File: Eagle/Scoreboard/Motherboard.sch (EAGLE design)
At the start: 24 parts

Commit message: Changed transistor type for score controller, changed number of terminals to 8. Motherboard still TBD
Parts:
- removed DISP_POWER: (no value), con-wago-500:W237-102
- added 12V, LED: (no value), con-wago-500:W237-102
- added R7: 470, resistor:R-EU_0204/5
- added SG1: EB2505, buzzer:EB2505
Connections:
- new net 12V: 12V-1.KL, 12V-2.KL, C1.+, R7.2, REG.VI, VCC-1.KL
- net GND: now also LED-1.KL; no longer DISP_POWER-1.KL
- net N$7: now also LED-2.KL, R7.1; no longer C1.+, REG.VI, VCC-1.KL
- net VCC: no longer DISP_POWER-2.KL

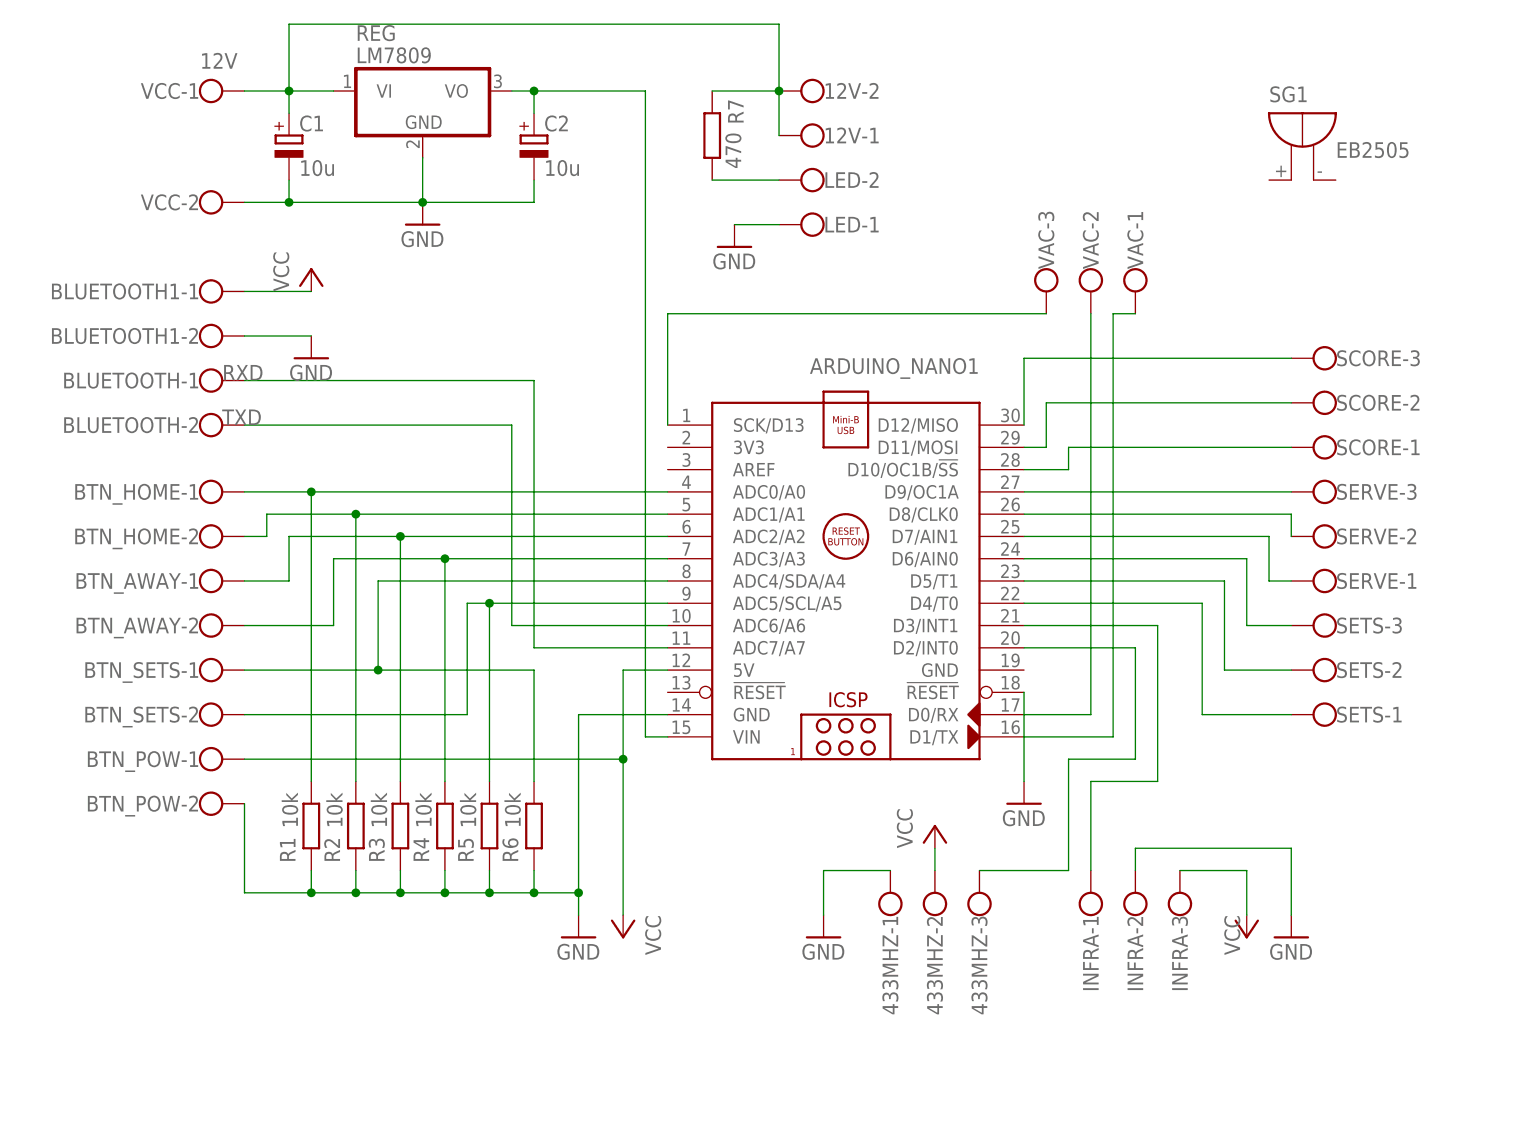
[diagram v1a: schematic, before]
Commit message: Changed matherboard scheme and start designing PCB
Scheme was changed to make easier PCB design. Still need to finish VCC layer on TOP layer
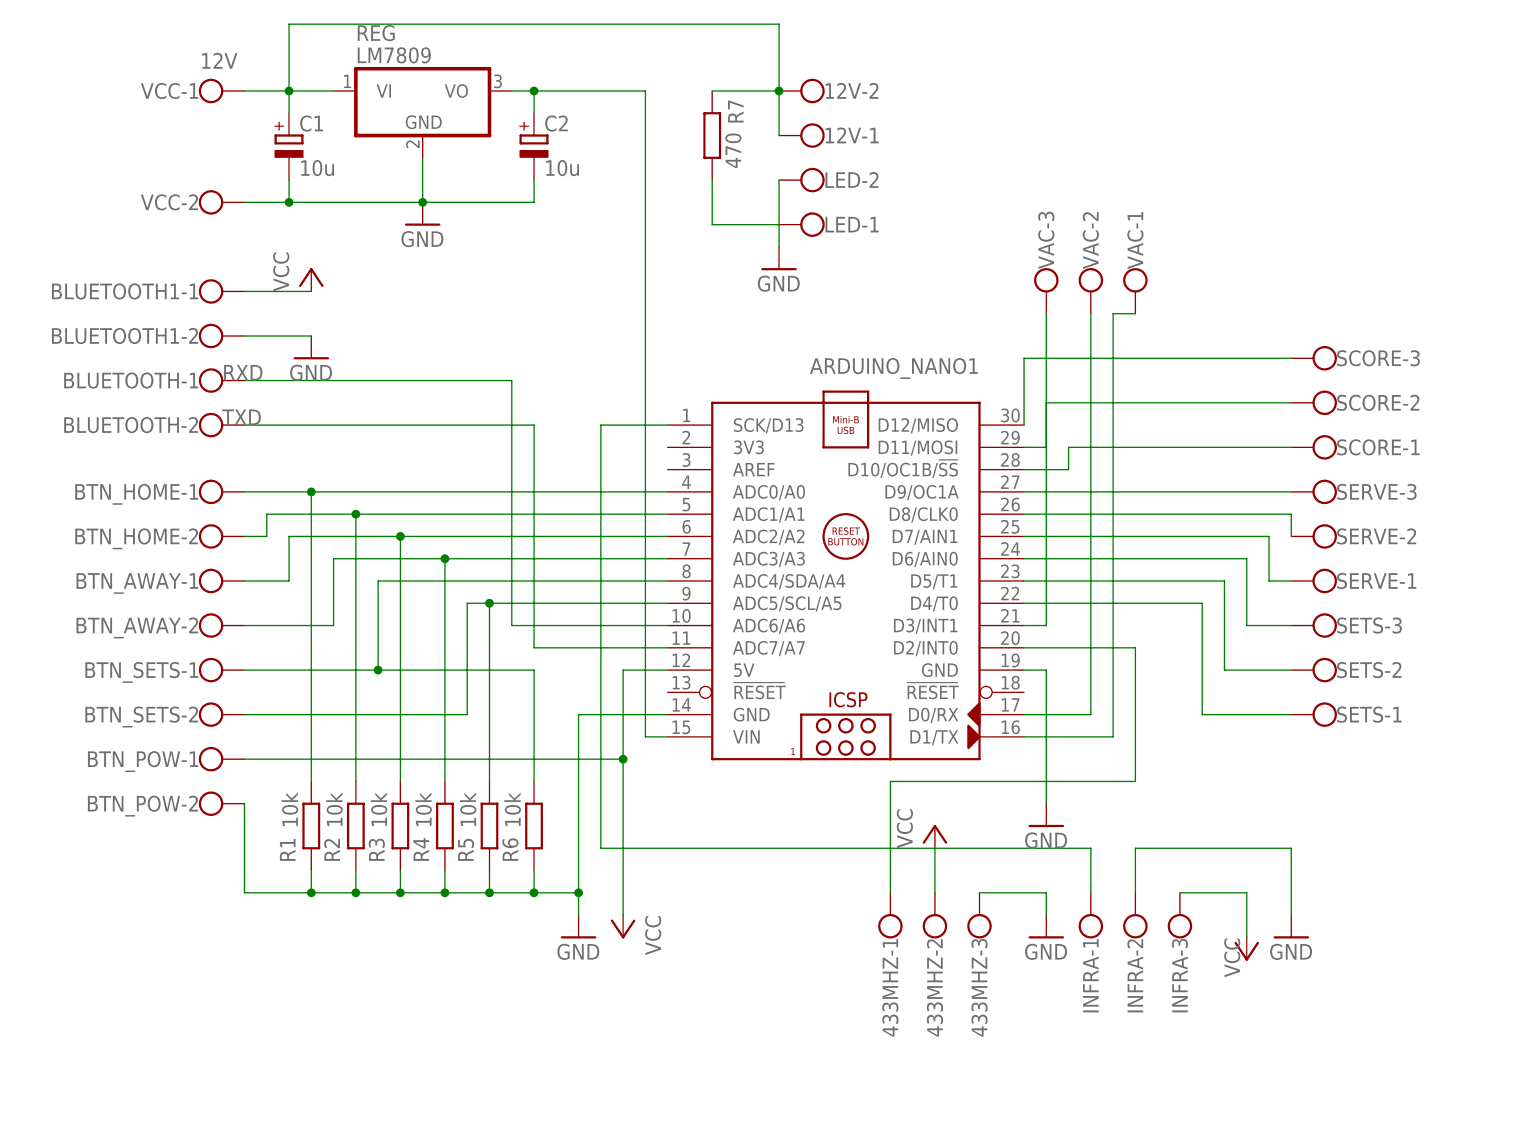
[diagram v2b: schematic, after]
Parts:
- removed SG1: EB2505, buzzer:EB2505
- R1, R2, R3, R4, R5, R6, R7: device resistor:R-EU_0204/5 -> resistor:R-EU_0204/7
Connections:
- net N$22 renamed VAC1
- net N$23 renamed VAC2
- removed net N$19: 433MHZ-3.KL, ARDUINO_NANO1.D2/INT0
- removed net N$20: ARDUINO_NANO1.D3/INT1, INFRA-1.KL
- removed net N$24: ARDUINO_NANO1.SCK/D13, VAC-3.KL
- removed net N$8: ARDUINO_NANO1.ADC6/A6, BLUETOOTH-2.KL
- removed net N$9: ARDUINO_NANO1.ADC7/A7, BLUETOOTH-1.KL
- new net 433MHZ: 433MHZ-1.KL, ARDUINO_NANO1.D2/INT0
- new net INFRA: ARDUINO_NANO1.SCK/D13, INFRA-1.KL
- new net RXD: ARDUINO_NANO1.ADC7/A7, BLUETOOTH-2.KL
- new net TXD: ARDUINO_NANO1.ADC6/A6, BLUETOOTH-1.KL
- new net VAC3: ARDUINO_NANO1.D3/INT1, VAC-3.KL
- net GND: now also 433MHZ-3.KL, ARDUINO_NANO1.GND@1, LED-2.KL; no longer 433MHZ-1.KL, ARDUINO_NANO1.!RESET@1, LED-1.KL
- net N$7: now also LED-1.KL; no longer LED-2.KL
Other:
- moved on the sheet: 433MHZ-1, 433MHZ-2, 433MHZ-3, INFRA-1, INFRA-2, INFRA-3

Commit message: Finalized board for motherboard
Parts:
- removed 433MHZ, INFRA: (no value), con-wago-500:W237-103
- added 433MHZ_VC, INFRA_VC, SIGNAL_IN: (no value), con-wago-500:W237-102
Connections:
- net N$10 renamed SCORE_3
- net N$11 renamed SCORE_2
- net N$12 renamed SCORE_1
- net N$13 renamed SERVE_3
- net N$14 renamed SERVE_2
- net N$15 renamed SERVE_1
- net N$16 renamed SETS_3
- net N$17 renamed SETS_2
- net N$18 renamed SETS_1
- net VIN renamed VIN_9V
- removed net VAC2: ARDUINO_NANO1.D0/RX, VAC-2.KL
- new net RESET: ARDUINO_NANO1.!RESET@1, VAC-2.KL
- net 433MHZ: now also SIGNAL_IN-1.KL; no longer 433MHZ-1.KL
- net GND: now also 433MHZ_VC-1.KL, INFRA_VC-2.KL; no longer 433MHZ-3.KL, INFRA-2.KL
- net INFRA: now also SIGNAL_IN-2.KL; no longer INFRA-1.KL
- net VCC: now also 433MHZ_VC-2.KL, INFRA_VC-1.KL; no longer 433MHZ-2.KL, INFRA-3.KL
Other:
- note added: "433 MHz"
- note added: "Infra"
- moved on the sheet: VAC-1, VAC-2, VAC-3

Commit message: Added capacitors for filtering
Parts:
- added C3, C4: 100n, capacitor-wima:C5/2.5
- C2: value 10u -> 47u
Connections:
- net 12V: now also C3.1
- net GND: now also C3.2, C4.2
- net VIN_9V: now also C4.1
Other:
- moved on the sheet: C1
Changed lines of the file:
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@@
 <part name="GND2" library="supply1" library_urn="urn:adsk.eagle:library:371" deviceset="GND" device=""/>
 <part name="C1" library="rcl" library_urn="urn:adsk.eagle:library:334" deviceset="CPOL-EU" device="E2-4" package3d_urn="urn:adsk.eagle:package:23347/1" value="10u"/>
-<part name="C2" library="rcl" library_urn="urn:adsk.eagle:library:334" deviceset="CPOL-EU" device="E2-4" package3d_urn="urn:adsk.eagle:package:23347/1" value="10u"/>
+<part name="C2" library="rcl" library_urn="urn:adsk.eagle:library:334" deviceset="CPOL-EU" device="E2-4" package3d_urn="urn:adsk.eagle:package:23347/1" value="47u"/>
 <part name="BLUETOOTH" library="con-wago-500" library_urn="urn:adsk.eagle:library:195" deviceset="W237-102" device="" package3d_urn="urn:adsk.eagle:package:10688/1"/>
 <part name="BLUETOOTH1" library="con-wago-500" library_urn="urn:adsk.eagle:library:195" deviceset="W237-102" device="" package3d_urn="urn:adsk.eagle:package:10688/1"/>
@@
 <part name="INFRA_VC" library="con-wago-500" library_urn="urn:adsk.eagle:library:195" deviceset="W237-102" device="" package3d_urn="urn:adsk.eagle:package:10688/1"/>
 <part name="433MHZ_VC" library="con-wago-500" library_urn="urn:adsk.eagle:library:195" deviceset="W237-102" device="" package3d_urn="urn:adsk.eagle:package:10688/1"/>
+<part name="C3" library="capacitor-wima" library_urn="urn:adsk.eagle:library:116" deviceset="C" device="5/2.5" package3d_urn="urn:adsk.eagle:package:5426/1" value="100n"/>
+<part name="C4" library="capacitor-wima" library_urn="urn:adsk.eagle:library:116" deviceset="C" device="5/2.5" package3d_urn="urn:adsk.eagle:package:5426/1" value="100n"/>
 </parts>
 <sheets>
@@
 <instance part="GND1" gate="1" x="0" y="93.98"/>
 <instance part="GND2" gate="1" x="17.78" y="12.7"/>
-<instance part="C1" gate="G$1" x="-15.24" y="104.14"/>
+<instance part="C1" gate="G$1" x="-12.7" y="104.14"/>
 <instance part="C2" gate="G$1" x="12.7" y="104.14"/>
 <instance part="BLUETOOTH" gate="-1" x="-25.4" y="76.2"/>
@@
 <instance part="433MHZ_VC" gate="-1" x="81.28" y="12.7" rot="R90"/>
 <instance part="433MHZ_VC" gate="-2" x="86.36" y="12.7" rot="R90"/>
+<instance part="C3" gate="G$1" x="-20.32" y="104.14"/>
+<instance part="C4" gate="G$1" x="20.32" y="104.14"/>
 </instances>
 <busses>
@@
 <pinref part="VCC" gate="-1" pin="KL"/>
 <pinref part="REG" gate="A1" pin="VI"/>
-<wire x1="-20.32" y1="109.22" x2="-15.24" y2="109.22" width="0.1524" layer="91"/>
-<wire x1="-15.24" y1="109.22" x2="-10.16" y2="109.22" width="0.1524" layer="91"/>
-<wire x1="-15.24" y1="106.68" x2="-15.24" y2="109.22" width="0.1524" layer="91"/>
-<junction x="-15.24" y="109.22"/>
+<wire x1="-20.32" y1="109.22" x2="-12.7" y2="109.22" width="0.1524" layer="91"/>
+<wire x1="-12.7" y1="109.22" x2="-10.16" y2="109.22" width="0.1524" layer="91"/>
+<wire x1="-12.7" y1="106.68" x2="-12.7" y2="109.22" width="0.1524" layer="91"/>
+<junction x="-12.7" y="109.22"/>
 <pinref part="C1" gate="G$1" pin="+"/>
 <label x="-25.4" y="111.76" size="1.778" layer="95"/>
@@
 <wire x1="40.64" y1="109.22" x2="40.64" y2="116.84" width="0.1524" layer="91"/>
 <junction x="40.64" y="109.22"/>
-<wire x1="40.64" y1="116.84" x2="-15.24" y2="116.84" width="0.1524" layer="91"/>
-<wire x1="-15.24" y1="116.84" x2="-15.24" y2="109.22" width="0.1524" layer="91"/>
+<wire x1="40.64" y1="116.84" x2="-12.7" y2="116.84" width="0.1524" layer="91"/>
+<wire x1="-12.7" y1="116.84" x2="-12.7" y2="109.22" width="0.1524" layer="91"/>
 <pinref part="R7" gate="G$1" pin="2"/>
 <wire x1="40.64" y1="109.22" x2="33.02" y2="109.22" width="0.1524" layer="91"/>
+<pinref part="C3" gate="G$1" pin="1"/>
+<wire x1="-20.32" y1="106.68" x2="-20.32" y2="109.22" width="0.1524" layer="91"/>
+<junction x="-20.32" y="109.22"/>
 </segment>
 </net>
@@
 <pinref part="VCC" gate="-2" pin="KL"/>
 <wire x1="0" y1="101.6" x2="0" y2="96.52" width="0.1524" layer="91"/>
-<wire x1="0" y1="96.52" x2="-15.24" y2="96.52" width="0.1524" layer="91"/>
+<wire x1="0" y1="96.52" x2="-12.7" y2="96.52" width="0.1524" layer="91"/>
 <pinref part="GND1" gate="1" pin="GND"/>
-<wire x1="-15.24" y1="96.52" x2="-20.32" y2="96.52" width="0.1524" layer="91"/>
+<wire x1="-12.7" y1="96.52" x2="-20.32" y2="96.52" width="0.1524" layer="91"/>
 <junction x="0" y="96.52"/>
-<wire x1="-15.24" y1="99.06" x2="-15.24" y2="96.52" width="0.1524" layer="91"/>
-<junction x="-15.24" y="96.52"/>
+<wire x1="-12.7" y1="99.06" x2="-12.7" y2="96.52" width="0.1524" layer="91"/>
+<junction x="-12.7" y="96.52"/>
 <wire x1="12.7" y1="99.06" x2="12.7" y2="96.52" width="0.1524" layer="91"/>
 <wire x1="12.7" y1="96.52" x2="0" y2="96.52" width="0.1524" layer="91"/>
 <pinref part="C1" gate="G$1" pin="-"/>
 <pinref part="C2" gate="G$1" pin="-"/>
+<pinref part="C3" gate="G$1" pin="2"/>
+<wire x1="-20.32" y1="99.06" x2="-20.32" y2="96.52" width="0.1524" layer="91"/>
+<junction x="-20.32" y="96.52"/>
+<pinref part="C4" gate="G$1" pin="2"/>
+<wire x1="20.32" y1="99.06" x2="20.32" y2="96.52" width="0.1524" layer="91"/>
+<wire x1="20.32" y1="96.52" x2="12.7" y2="96.52" width="0.1524" layer="91"/>
+<junction x="12.7" y="96.52"/>
 </segment>
 <segment>
@@
 <wire x1="12.7" y1="106.68" x2="12.7" y2="109.22" width="0.1524" layer="91"/>
 <pinref part="C2" gate="G$1" pin="+"/>
-<wire x1="12.7" y1="109.22" x2="25.4" y2="109.22" width="0.1524" layer="91"/>
+<wire x1="12.7" y1="109.22" x2="20.32" y2="109.22" width="0.1524" layer="91"/>
+<wire x1="20.32" y1="109.22" x2="25.4" y2="109.22" width="0.1524" layer="91"/>
 <wire x1="25.4" y1="109.22" x2="25.4" y2="35.56" width="0.1524" layer="91"/>
 <junction x="12.7" y="109.22"/>
 <pinref part="ARDUINO_NANO1" gate="G$1" pin="VIN"/>
 <wire x1="25.4" y1="35.56" x2="27.94" y2="35.56" width="0.1524" layer="91"/>
-</segment>
-</net>
+<pinref part="C4" gate="G$1" pin="1"/>
+<wire x1="20.32" y1="106.68" x2="20.32" y2="109.22" width="0.1524" layer="91"/>
+<junction x="20.32" y="109.22"/>
+</segment>
+</net>

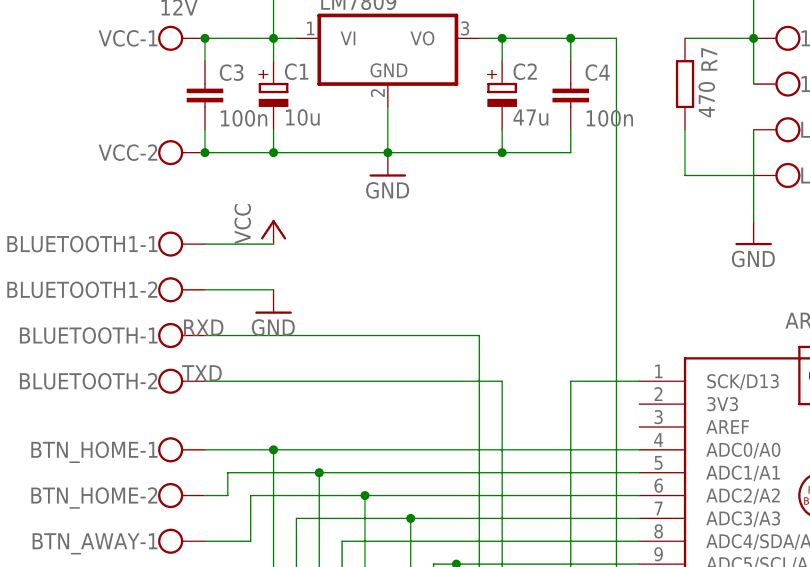
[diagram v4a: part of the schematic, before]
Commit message: Added polygon and make more space for screws
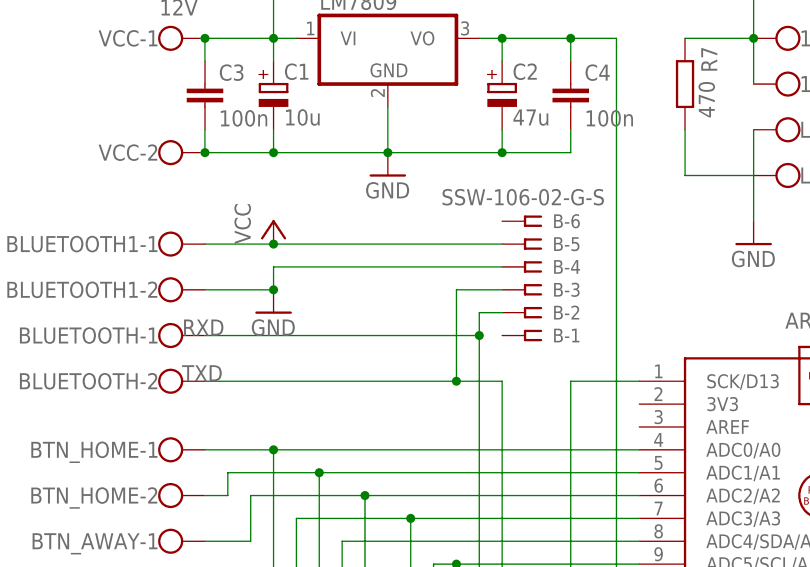
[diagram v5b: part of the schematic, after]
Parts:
- added B: SSW-106-02-G-S, con-samtec:SSW-106-02-G-S
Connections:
- net GND: now also B-4.1
- net RXD: now also ARDUINO_NANO1.ADC6/A6, B-2.1, BLUETOOTH-1.KL; no longer ARDUINO_NANO1.ADC7/A7, BLUETOOTH-2.KL
- net TXD: now also ARDUINO_NANO1.ADC7/A7, B-3.1, BLUETOOTH-2.KL; no longer ARDUINO_NANO1.ADC6/A6, BLUETOOTH-1.KL
- net VCC: now also B-5.1
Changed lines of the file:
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@@
 <part name="C3" library="capacitor-wima" library_urn="urn:adsk.eagle:library:116" deviceset="C" device="5/2.5" package3d_urn="urn:adsk.eagle:package:5426/1" value="100n"/>
 <part name="C4" library="capacitor-wima" library_urn="urn:adsk.eagle:library:116" deviceset="C" device="5/2.5" package3d_urn="urn:adsk.eagle:package:5426/1" value="100n"/>
+<part name="B" library="con-samtec" library_urn="urn:adsk.eagle:library:184" deviceset="SSW-106-02-G-S" device=""/>
 </parts>
 <sheets>
@@
 <instance part="C3" gate="G$1" x="-20.32" y="104.14"/>
 <instance part="C4" gate="G$1" x="20.32" y="104.14"/>
+<instance part="B" gate="-1" x="15.24" y="76.2" smashed="yes" rot="R180">
+<attribute name="VALUE" x="24.13" y="92.456" size="1.778" layer="96" rot="R180"/>
+<attribute name="NAME" x="18.288" y="75.438" size="1.524" layer="95"/>
+</instance>
+<instance part="B" gate="-2" x="15.24" y="78.74" rot="R180"/>
+<instance part="B" gate="-3" x="15.24" y="81.28" rot="R180"/>
+<instance part="B" gate="-4" x="15.24" y="83.82" rot="R180"/>
+<instance part="B" gate="-5" x="15.24" y="86.36" rot="R180"/>
+<instance part="B" gate="-6" x="15.24" y="88.9" rot="R180"/>
 </instances>
 <busses>
@@
 <pinref part="GND3" gate="1" pin="GND"/>
 <wire x1="-20.32" y1="81.28" x2="-12.7" y2="81.28" width="0.1524" layer="91"/>
+<pinref part="B" gate="-4" pin="1"/>
+<wire x1="12.7" y1="83.82" x2="-12.7" y2="83.82" width="0.1524" layer="91"/>
+<wire x1="-12.7" y1="83.82" x2="-12.7" y2="81.28" width="0.1524" layer="91"/>
+<junction x="-12.7" y="81.28"/>
 </segment>
 <segment>
@@
 </segment>
 </net>
-<net name="TXD" class="0">
+<net name="RXD" class="0">
 <segment>
 <pinref part="ARDUINO_NANO1" gate="G$1" pin="ADC6/A6"/>
@@
 <wire x1="-20.32" y1="76.2" x2="10.16" y2="76.2" width="0.1524" layer="91"/>
 <wire x1="10.16" y1="76.2" x2="10.16" y2="71.12" width="0.1524" layer="91"/>
-</segment>
-</net>
-<net name="RXD" class="0">
+<pinref part="B" gate="-2" pin="1"/>
+<wire x1="12.7" y1="78.74" x2="10.16" y2="78.74" width="0.1524" layer="91"/>
+<wire x1="10.16" y1="78.74" x2="10.16" y2="76.2" width="0.1524" layer="91"/>
+<junction x="10.16" y="76.2"/>
+</segment>
+</net>
+<net name="TXD" class="0">
 <segment>
 <pinref part="ARDUINO_NANO1" gate="G$1" pin="ADC7/A7"/>
@@
 <wire x1="27.94" y1="45.72" x2="12.7" y2="45.72" width="0.1524" layer="91"/>
 <pinref part="BLUETOOTH" gate="-2" pin="KL"/>
-<wire x1="-20.32" y1="71.12" x2="12.7" y2="71.12" width="0.1524" layer="91"/>
+<wire x1="-20.32" y1="71.12" x2="7.62" y2="71.12" width="0.1524" layer="91"/>
+<pinref part="B" gate="-3" pin="1"/>
+<wire x1="7.62" y1="71.12" x2="12.7" y2="71.12" width="0.1524" layer="91"/>
+<wire x1="12.7" y1="81.28" x2="7.62" y2="81.28" width="0.1524" layer="91"/>
+<wire x1="7.62" y1="81.28" x2="7.62" y2="71.12" width="0.1524" layer="91"/>
+<junction x="7.62" y="71.12"/>
 </segment>
 </net>
@@
 <wire x1="-20.32" y1="86.36" x2="-12.7" y2="86.36" width="0.1524" layer="91"/>
 <pinref part="P+2" gate="VCC" pin="VCC"/>
-</segment>
-<segment>
+<pinref part="B" gate="-5" pin="1"/>
+<wire x1="12.7" y1="86.36" x2="-12.7" y2="86.36" width="0.1524" layer="91"/>
+<junction x="-12.7" y="86.36"/>
+</segment>
+<segment>
